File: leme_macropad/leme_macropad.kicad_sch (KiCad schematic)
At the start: 36 parts, among them J1 USB_C_Receptacle_USB2.0_16P, U1 SRV05-4HTG-D, U2 NCP1117-3.3_SOT223

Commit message: Assigns footprints to all components in schematics
Passives are 0603, but if the layout gets too dificult (specially around
the RP2040) we might want to decrease the size.

The mechanical switches are set as hotswap sockets for Kailh v1/v2, but
after routing everything we might want to do a version for MX switches.
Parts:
- C1, C2: footprint (none) -> Capacitor_SMD:C_0603_1608Metric_Pad1.08x0.95mm_HandSolder
- J1: footprint (none) -> Connector_USB:USB_C_Receptacle_GCT_USB4105-xx-A_16P_TopMnt_Horizontal
- R1, R2: footprint (none) -> Resistor_SMD:R_0603_1608Metric_Pad0.98x0.95mm_HandSolder
- TP1, TP10, TP11, TP12, TP13, TP14, TP15, TP16, TP17, TP18, TP19, TP2, TP20, TP21, TP22, TP23, TP24, TP25, TP26, TP27, TP28, TP29, TP3, TP4, TP5, TP6, TP7, TP8, TP9: footprint (none) -> TestPoint:TestPoint_Pad_D2.0mm
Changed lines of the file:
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@@
 			)
 		)
-		(property "Footprint" ""
+		(property "Footprint" "TestPoint:TestPoint_Pad_D2.0mm"
 			(at 88.9 179.07 0)
 			(effects
@@
 			)
 		)
-		(property "Footprint" ""
+		(property "Footprint" "TestPoint:TestPoint_Pad_D2.0mm"
 			(at 88.9 160.02 0)
 			(effects
@@
 			)
 		)
-		(property "Footprint" ""
+		(property "Footprint" "TestPoint:TestPoint_Pad_D2.0mm"
 			(at 54.61 161.29 0)
 			(effects
@@
 			)
 		)
-		(property "Footprint" ""
+		(property "Footprint" "TestPoint:TestPoint_Pad_D2.0mm"
 			(at 161.29 168.91 0)
 			(effects
@@
 			)
 		)
-		(property "Footprint" ""
+		(property "Footprint" "TestPoint:TestPoint_Pad_D2.0mm"
 			(at 22.86 175.26 0)
 			(effects
@@
 			)
 		)
-		(property "Footprint" ""
+		(property "Footprint" "TestPoint:TestPoint_Pad_D2.0mm"
 			(at 54.61 182.88 0)
 			(effects
@@
 			)
 		)
-		(property "Footprint" ""
+		(property "Footprint" "Connector_USB:USB_C_Receptacle_GCT_USB4105-xx-A_16P_TopMnt_Horizontal"
 			(at 36.83 50.8 0)
 			(effects
@@
 			)
 		)
-		(property "Footprint" ""
+		(property "Footprint" "TestPoint:TestPoint_Pad_D2.0mm"
 			(at 88.9 163.83 0)
 			(effects
@@
 			)
 		)
-		(property "Footprint" ""
+		(property "Footprint" "TestPoint:TestPoint_Pad_D2.0mm"
 			(at 54.61 179.07 0)
 			(effects
@@
 			)
 		)
-		(property "Footprint" ""
+		(property "Footprint" "TestPoint:TestPoint_Pad_D2.0mm"
 			(at 54.61 173.99 0)
 			(effects
@@
 			)
 		)
-		(property "Footprint" ""
+		(property "Footprint" "TestPoint:TestPoint_Pad_D2.0mm"
 			(at 88.9 167.64 0)
 			(effects
@@
 			)
 		)
-		(property "Footprint" ""
+		(property "Footprint" "TestPoint:TestPoint_Pad_D2.0mm"
 			(at 123.19 160.02 0)
 			(effects
@@
 			)
 		)
-		(property "Footprint" ""
+		(property "Footprint" "TestPoint:TestPoint_Pad_D2.0mm"
 			(at 175.26 185.42 0)
 			(effects
@@
 			)
 		)
-		(property "Footprint" ""
+		(property "Footprint" "Resistor_SMD:R_0603_1608Metric_Pad0.98x0.95mm_HandSolder"
 			(at 54.61 43.18 0)
 			(effects
@@
 			)
 		)
-		(property "Footprint" ""
+		(property "Footprint" "TestPoint:TestPoint_Pad_D2.0mm"
 			(at 54.61 170.18 0)
 			(effects
@@
 			)
 		)
-		(property "Footprint" ""
+		(property "Footprint" "TestPoint:TestPoint_Pad_D2.0mm"
 			(at 123.19 167.64 0)
 			(effects
@@
 			)
 		)
-		(property "Footprint" ""
+		(property "Footprint" "TestPoint:TestPoint_Pad_D2.0mm"
 			(at 88.9 175.26 0)
 			(effects
@@
 			)
 		)
-		(property "Footprint" ""
+		(property "Footprint" "TestPoint:TestPoint_Pad_D2.0mm"
 			(at 54.61 165.1 0)
 			(effects
@@
 			)
 		)
-		(property "Footprint" ""
+		(property "Footprint" "Capacitor_SMD:C_0603_1608Metric_Pad1.08x0.95mm_HandSolder"
 			(at 147.32 38.1 0)
 			(effects
@@
 			)
 		)
-		(property "Footprint" ""
+		(property "Footprint" "TestPoint:TestPoint_Pad_D2.0mm"
 			(at 88.9 182.88 0)
 			(effects
@@
 			)
 		)
-		(property "Footprint" ""
+		(property "Footprint" "TestPoint:TestPoint_Pad_D2.0mm"
 			(at 123.19 182.88 0)
 			(effects
@@
 			)
 		)
-		(property "Footprint" ""
+		(property "Footprint" "TestPoint:TestPoint_Pad_D2.0mm"
 			(at 123.19 156.21 0)
 			(effects
@@
 			)
 		)
-		(property "Footprint" ""
+		(property "Footprint" "TestPoint:TestPoint_Pad_D2.0mm"
 			(at 123.19 179.07 0)
 			(effects
@@
 			)
 		)
-		(property "Footprint" ""
+		(property "Footprint" "TestPoint:TestPoint_Pad_D2.0mm"
 			(at 157.48 185.42 0)
 			(effects
@@
 			)
 		)
-		(property "Footprint" ""
+		(property "Footprint" "TestPoint:TestPoint_Pad_D2.0mm"
 			(at 151.13 168.91 0)
 			(effects
@@
 			)
 		)
-		(property "Footprint" ""
+		(property "Footprint" "TestPoint:TestPoint_Pad_D2.0mm"
 			(at 22.86 182.88 0)
 			(effects
@@
 			)
 		)
-		(property "Footprint" ""
+		(property "Footprint" "TestPoint:TestPoint_Pad_D2.0mm"
 			(at 22.86 179.07 0)
 			(effects
@@
 			)
 		)
-		(property "Footprint" ""
+		(property "Footprint" "TestPoint:TestPoint_Pad_D2.0mm"
 			(at 123.19 171.45 0)
 			(effects
@@
 			)
 		)
-		(property "Footprint" ""
+		(property "Footprint" "Capacitor_SMD:C_0603_1608Metric_Pad1.08x0.95mm_HandSolder"
 			(at 116.84 38.1 0)
 			(effects
@@
 			)
 		)
-		(property "Footprint" ""
+		(property "Footprint" "TestPoint:TestPoint_Pad_D2.0mm"
 			(at 88.9 171.45 0)
 			(effects
@@
 			)
 		)
-		(property "Footprint" ""
+		(property "Footprint" "TestPoint:TestPoint_Pad_D2.0mm"
 			(at 123.19 175.26 0)
 			(effects
@@
 			)
 		)
-		(property "Footprint" ""
+		(property "Footprint" "Resistor_SMD:R_0603_1608Metric_Pad0.98x0.95mm_HandSolder"
 			(at 54.61 40.64 0)
 			(effects
@@
 			)
 		)
-		(property "Footprint" ""
+		(property "Footprint" "TestPoint:TestPoint_Pad_D2.0mm"
 			(at 166.37 185.42 0)
 			(effects
@@
 			)
 		)
-		(property "Footprint" ""
+		(property "Footprint" "TestPoint:TestPoint_Pad_D2.0mm"
 			(at 88.9 156.21 0)
 			(effects

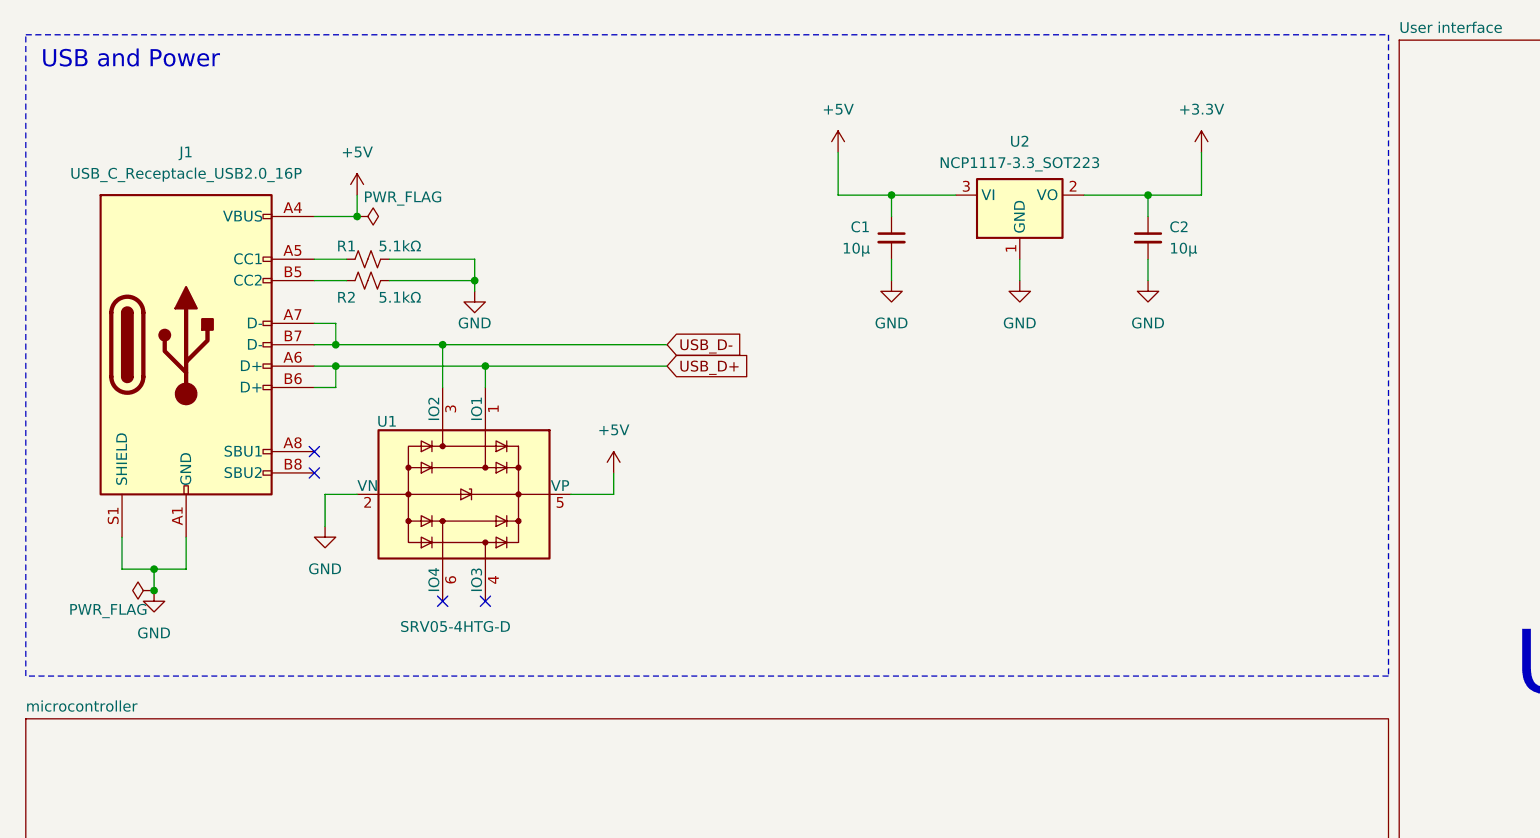
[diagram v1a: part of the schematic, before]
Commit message: Adds M2 mounting holes to schematics
The mounting holes are pads and connected to ground.
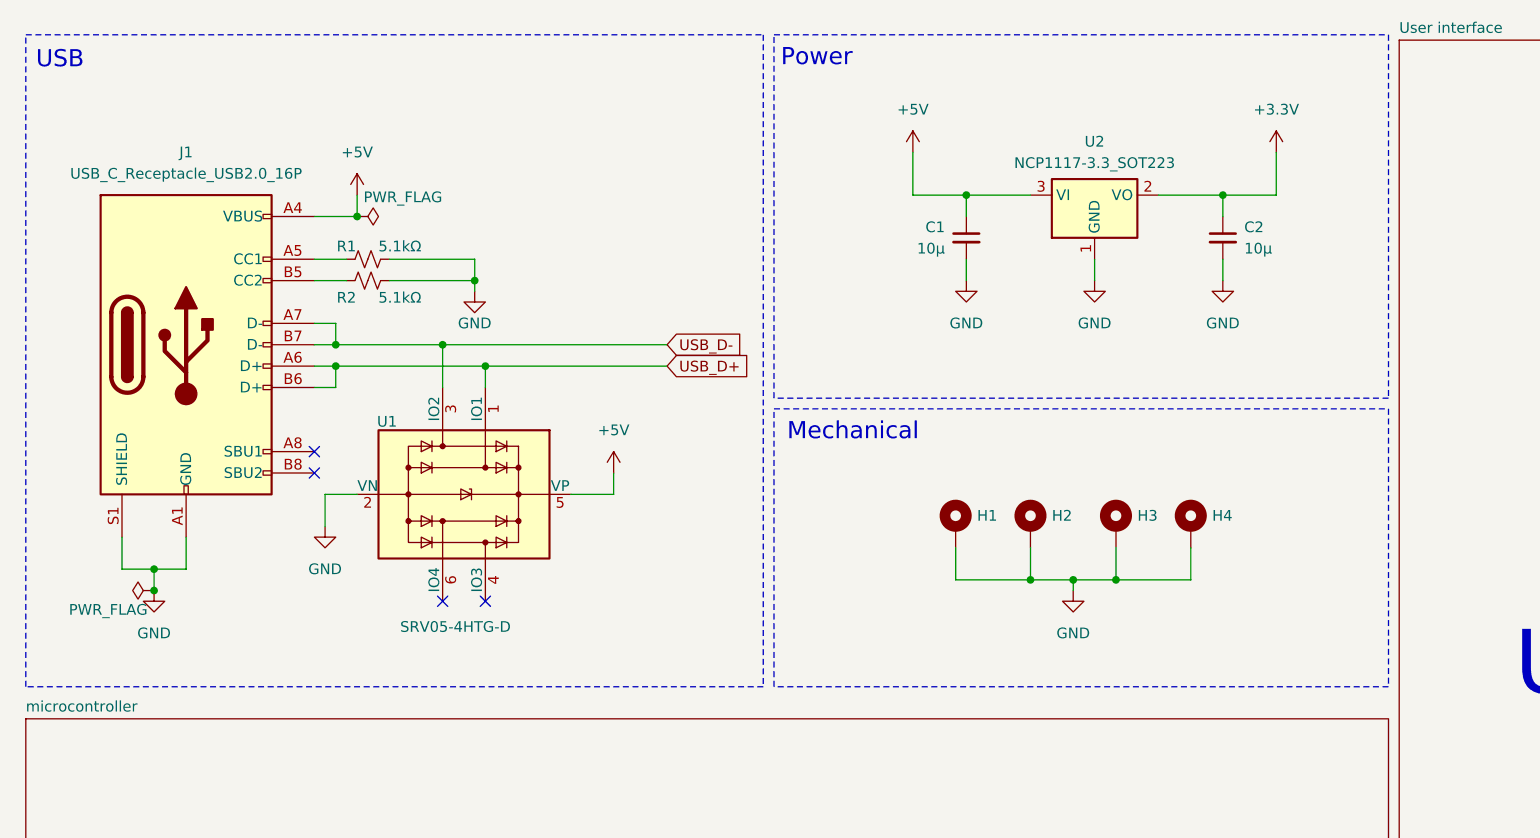
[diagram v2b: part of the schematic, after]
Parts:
- added H1, H2, H3, H4: MountingHole_Pad, MountingHole:MountingHole_2.2mm_M2_Pad, symbol Mechanical:MountingHole_Pad
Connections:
- net GND: now also H1.1, H2.1, H3.1, H4.1
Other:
- note added: "Mechanical"
- note added: "Power"
- note added: "USB"
- note removed: "USB and Power"
- moved on the sheet: C1, C2, U2

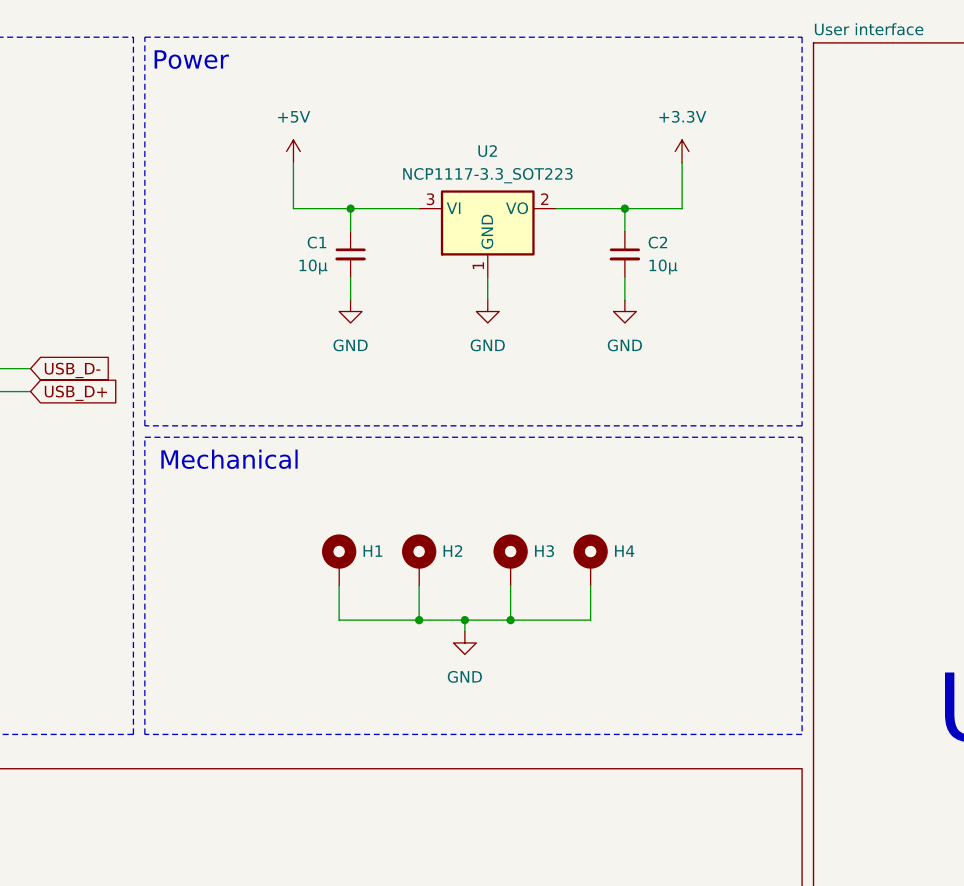
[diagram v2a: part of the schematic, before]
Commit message: Adds logo to schematics
This includes a symbol and a footprint. The logo is a pad, connected to
ground.
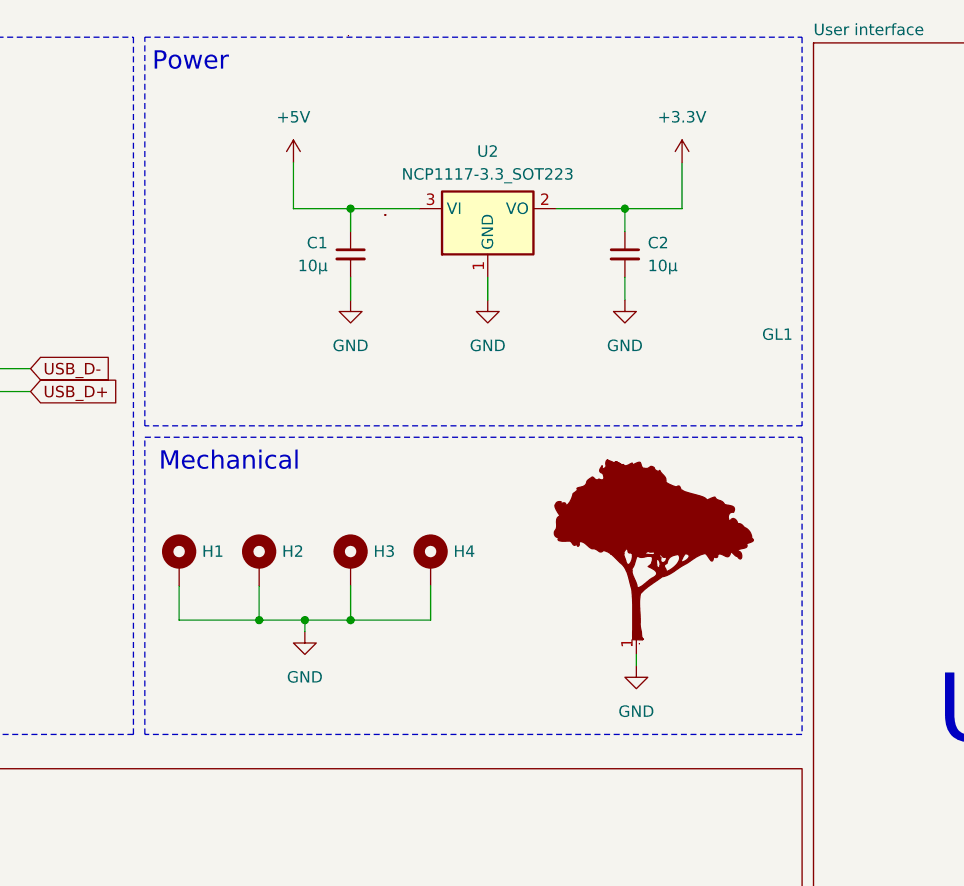
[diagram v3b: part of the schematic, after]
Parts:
- added GL1: ~, leme_macropad:ipe_logo, symbol ipe_logo:Ipe_logo
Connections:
- net GND: now also GL1.1
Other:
- moved on the sheet: H1, H2, H3, H4
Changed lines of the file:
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@@
 	)
 	(junction
-		(at 143.51 78.74)
+		(at 125.73 78.74)
 		(diameter 0)
 		(color 0 0 0 0)
 	)
 	(junction
-		(at 133.35 78.74)
+		(at 115.57 78.74)
 		(diameter 0)
 		(color 0 0 0 0)
@@
 	)
 	(junction
-		(at 138.43 78.74)
+		(at 120.65 78.74)
 		(diameter 0)
 		(color 0 0 0 0)
@@
 	(wire
 		(pts
-			(xy 124.46 78.74) (xy 133.35 78.74)
+			(xy 106.68 78.74) (xy 115.57 78.74)
 		)
 		(stroke
@@
 	(wire
 		(pts
-			(xy 152.4 78.74) (xy 143.51 78.74)
+			(xy 134.62 78.74) (xy 125.73 78.74)
 		)
 		(stroke
@@
 	(wire
 		(pts
-			(xy 143.51 78.74) (xy 138.43 78.74)
+			(xy 125.73 78.74) (xy 120.65 78.74)
 		)
 		(stroke
@@
 	(wire
 		(pts
+			(xy 157.48 82.55) (xy 157.48 83.82)
+		)
+		(stroke
+			(width 0)
+			(type default)
+		)
+	)
+	(wire
+		(pts
 			(xy 127 180.34) (xy 123.19 180.34)
 		)
@@
 	(wire
 		(pts
-			(xy 143.51 74.93) (xy 143.51 78.74)
+			(xy 125.73 74.93) (xy 125.73 78.74)
 		)
 		(stroke
@@
 	(wire
 		(pts
-			(xy 133.35 78.74) (xy 138.43 78.74)
+			(xy 115.57 78.74) (xy 120.65 78.74)
 		)
 		(stroke
@@
 	(wire
 		(pts
-			(xy 133.35 74.93) (xy 133.35 78.74)
+			(xy 115.57 74.93) (xy 115.57 78.74)
 		)
 		(stroke
@@
 	(wire
 		(pts
-			(xy 152.4 74.93) (xy 152.4 78.74)
+			(xy 134.62 74.93) (xy 134.62 78.74)
 		)
 		(stroke
@@
 	(wire
 		(pts
-			(xy 138.43 78.74) (xy 138.43 80.01)
+			(xy 120.65 78.74) (xy 120.65 80.01)
 		)
 		(stroke
@@
 	(wire
 		(pts
-			(xy 124.46 74.93) (xy 124.46 78.74)
+			(xy 106.68 74.93) (xy 106.68 78.74)
 		)
 		(stroke
@@
 	(symbol
 		(lib_id "Mechanical:MountingHole_Pad")
-		(at 152.4 72.39 0)
+		(at 134.62 72.39 0)
 		(unit 1)
 		(exclude_from_sim no)
@@
 		(fields_autoplaced yes)
 		(property "Reference" "H4"
-			(at 154.94 71.1199 0)
+			(at 137.16 71.1199 0)
 			(effects
 				(font
@@
 		)
 		(property "Value" "MountingHole_Pad"
-			(at 154.94 72.3899 0)
+			(at 137.16 72.3899 0)
 			(effects
 				(font
@@
 		)
 		(property "Footprint" "MountingHole:MountingHole_2.2mm_M2_Pad"
-			(at 152.4 72.39 0)
+			(at 134.62 72.39 0)
 			(effects
 				(font
@@
 		)
 		(property "Datasheet" "~"
-			(at 152.4 72.39 0)
+			(at 134.62 72.39 0)
 			(effects
 				(font
@@
 		)
 		(property "Description" "Mounting Hole with connection"
-			(at 152.4 72.39 0)
+			(at 134.62 72.39 0)
 			(effects
 				(font
@@
 	(symbol
 		(lib_id "Mechanical:MountingHole_Pad")
-		(at 133.35 72.39 0)
+		(at 115.57 72.39 0)
 		(unit 1)
 		(exclude_from_sim no)
@@
 		(fields_autoplaced yes)
 		(property "Reference" "H2"
-			(at 135.89 71.1199 0)
+			(at 118.11 71.1199 0)
 			(effects
 				(font
@@
 		)
 		(property "Value" "MountingHole_Pad"
-			(at 135.89 72.3899 0)
+			(at 118.11 72.3899 0)
 			(effects
 				(font
@@
 		)
 		(property "Footprint" "MountingHole:MountingHole_2.2mm_M2_Pad"
-			(at 133.35 72.39 0)
+			(at 115.57 72.39 0)
 			(effects
 				(font
@@
 		)
 		(property "Datasheet" "~"
-			(at 133.35 72.39 0)
+			(at 115.57 72.39 0)
 			(effects
 				(font
@@
 		)
 		(property "Description" "Mounting Hole with connection"
-			(at 133.35 72.39 0)
+			(at 115.57 72.39 0)
 			(effects
 				(font
@@
 	(symbol
 		(lib_id "power:GND")
-		(at 138.43 80.01 0)
+		(at 120.65 80.01 0)
 		(unit 1)
 		(exclude_from_sim no)
@@
 		(fields_autoplaced yes)
 		(property "Reference" "#PWR061"
-			(at 138.43 86.36 0)
+			(at 120.65 86.36 0)
 			(effects
 				(font
@@
 		)
 		(property "Value" "GND"
-			(at 138.43 85.09 0)
+			(at 120.65 85.09 0)
 			(effects
 				(font
@@
 		)
 		(property "Footprint" ""
-			(at 138.43 80.01 0)
+			(at 120.65 80.01 0)
 			(effects
 				(font
@@
 		)
 		(property "Datasheet" ""
-			(at 138.43 80.01 0)
+			(at 120.65 80.01 0)
 			(effects
 				(font
@@
 		)
 		(property "Description" "Power symbol creates a global label with name \"GND\" , ground"
-			(at 138.43 80.01 0)
+			(at 120.65 80.01 0)
 			(effects
 				(font
@@
 	(symbol
 		(lib_id "Mechanical:MountingHole_Pad")
-		(at 143.51 72.39 0)
+		(at 125.73 72.39 0)
 		(unit 1)
 		(exclude_from_sim no)
@@
 		(fields_autoplaced yes)
 		(property "Reference" "H3"
-			(at 146.05 71.1199 0)
+			(at 128.27 71.1199 0)
 			(effects
 				(font
@@
 		)
 		(property "Value" "MountingHole_Pad"
-			(at 146.05 72.3899 0)
+			(at 128.27 72.3899 0)
 			(effects
 				(font
@@
 		)
 		(property "Footprint" "MountingHole:MountingHole_2.2mm_M2_Pad"
-			(at 143.51 72.39 0)
+			(at 125.73 72.39 0)
 			(effects
 				(font
@@
 		)
 		(property "Datasheet" "~"
-			(at 143.51 72.39 0)
+			(at 125.73 72.39 0)
 			(effects
 				(font
@@
 		)
 		(property "Description" "Mounting Hole with connection"
-			(at 143.51 72.39 0)
+			(at 125.73 72.39 0)
 			(effects
 				(font
@@
 	(symbol
 		(lib_id "Mechanical:MountingHole_Pad")
-		(at 124.46 72.39 0)
+		(at 106.68 72.39 0)
 		(unit 1)
 		(exclude_from_sim no)
@@
 		(fields_autoplaced yes)
 		(property "Reference" "H1"
-			(at 127 71.1199 0)
+			(at 109.22 71.1199 0)
 			(effects
 				(font
@@
 		)
 		(property "Value" "MountingHole_Pad"
-			(at 127 72.3899 0)
+			(at 109.22 72.3899 0)
 			(effects
 				(font
@@
 		)
 		(property "Footprint" "MountingHole:MountingHole_2.2mm_M2_Pad"
-			(at 124.46 72.39 0)
+			(at 106.68 72.39 0)
 			(effects
 				(font
@@
 		)
 		(property "Datasheet" "~"
-			(at 124.46 72.39 0)
+			(at 106.68 72.39 0)
 			(effects
 				(font
@@
 		)
 		(property "Description" "Mounting Hole with connection"
-			(at 124.46 72.39 0)
+			(at 106.68 72.39 0)
 			(effects
 				(font
@@
 	)
 	(symbol
+		(lib_id "ipe_logo:Ipe_logo")
+		(at 157.48 71.12 0)
+		(unit 1)
+		(exclude_from_sim no)
+		(in_bom no)
+		(on_board yes)
+		(dnp no)
+		(fields_autoplaced yes)
+		(property "Reference" "GL1"
+			(at 171.45 47.0084 0)
+			(effects
+				(font
+					(size 1.27 1.27)
+				)
+				(justify left)
+			)
+		)
+		(property "Value" "~"
+			(at 171.45 48.9135 0)
+			(effects
+				(font
+					(size 1.27 1.27)
+				)
+				(justify left)
+			)
+		)
+		(property "Footprint" "leme_macropad:ipe_logo"
+			(at 157.48 71.12 0)
+			(effects
+				(font
+					(size 1.27 1.27)
+				)
+				(hide yes)
+			)
+		)
+		(property "Datasheet" ""
+			(at 157.48 71.12 0)
+			(effects
+				(font
+					(size 1.27 1.27)
+				)
+				(hide yes)
+			)
+		)
+		(property "Description" ""
+			(at 157.48 71.12 0)
+			(effects
+				(font
+					(size 1.27 1.27)
+				)
+				(hide yes)
+			)
+		)
+		(pin "1"
+		)
+		(instances
+			(project ""
+				(path "/a37365a2-c635-4451-9354-78f9e753d687"
+					(reference "GL1")
+					(unit 1)
+				)
+			)
+		)
+	)
+	(symbol
 		(lib_id "Device:R_Small_US")
 		(at 54.61 40.64 90)
@@
 					(unit 1)
 				)
+			)
+		)
+	)
+	(symbol
+		(lib_id "power:GND")
+		(at 157.48 83.82 0)
+		(unit 1)
+		(exclude_from_sim no)
+		(in_bom yes)
+		(on_board yes)
+		(dnp no)
+		(fields_autoplaced yes)
+		(property "Reference" "#PWR062"
+			(at 157.48 90.17 0)
+			(effects
+				(font
+					(size 1.27 1.27)
+				)
+				(hide yes)
+			)
+		)
+		(property "Value" "GND"
+			(at 157.48 88.9 0)
+			(effects
+				(font
+					(size 1.27 1.27)
+				)
+			)
+		)
+		(property "Footprint" ""
+			(at 157.48 83.82 0)
+			(effects
+				(font
+					(size 1.27 1.27)
+				)
+				(hide yes)
+			)
+		)
+		(property "Datasheet" ""
+			(at 157.48 83.82 0)
+			(effects
+				(font
+					(size 1.27 1.27)
+				)
+				(hide yes)
+			)
+		)
+		(property "Description" "Power symbol creates a global label with name \"GND\" , ground"
+			(at 157.48 83.82 0)
+			(effects
+				(font
+					(size 1.27 1.27)
+				)
+				(hide yes)
+			)
+		)
+		(pin "1"
+		)
+		(instances
+			(project "leme_macropad"
+				(path "/a37365a2-c635-4451-9354-78f9e753d687"
+					(reference "#PWR062")
+					(unit 1)
+				)
